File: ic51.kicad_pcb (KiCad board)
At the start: 2 copper layers, 76.1 x 76 mm, 5 parts, among them J1 Conn_02x18_Odd_Even, J2 Conn_02x18_Odd_Even, J3 Conn_02x18_Odd_Even, J4 Conn_02x18_Odd_Even, U1 ic51-1444-schem

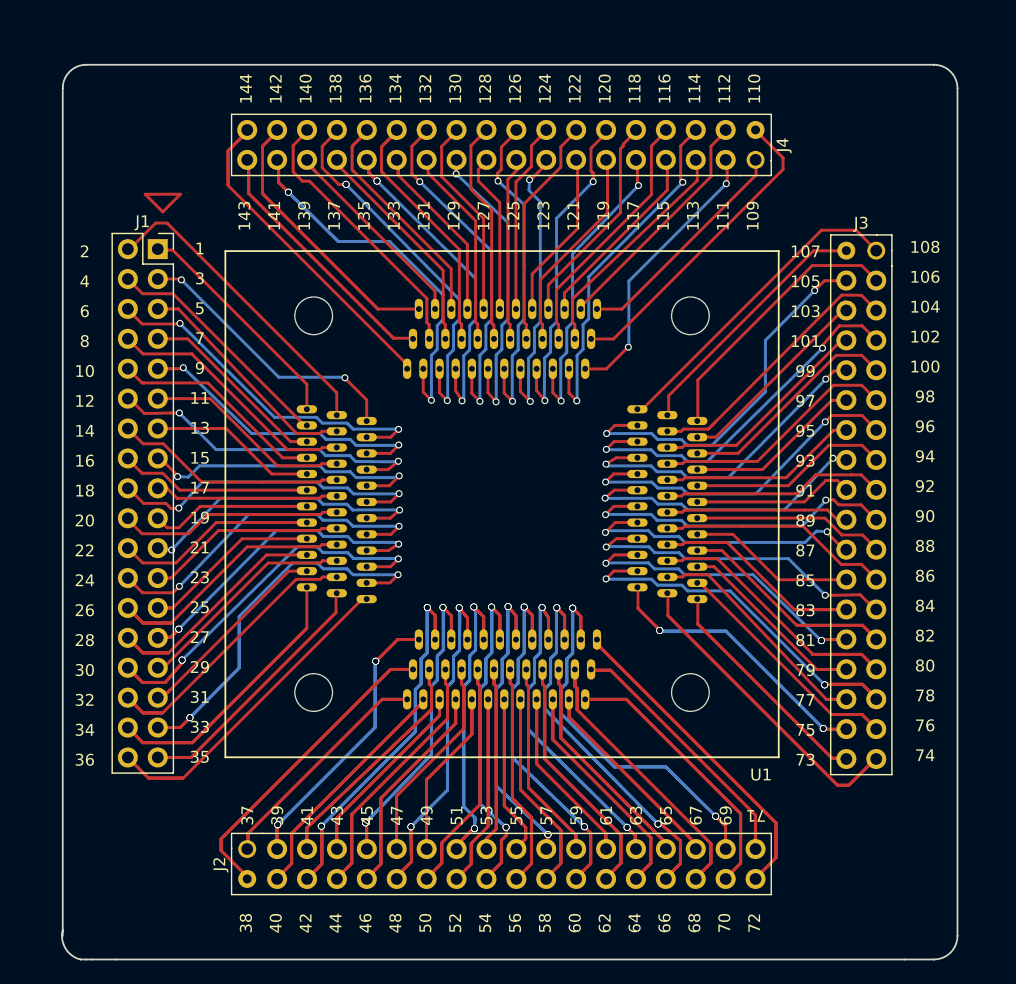
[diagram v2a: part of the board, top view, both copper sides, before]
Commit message: fill unused zones with copper, move align text properly
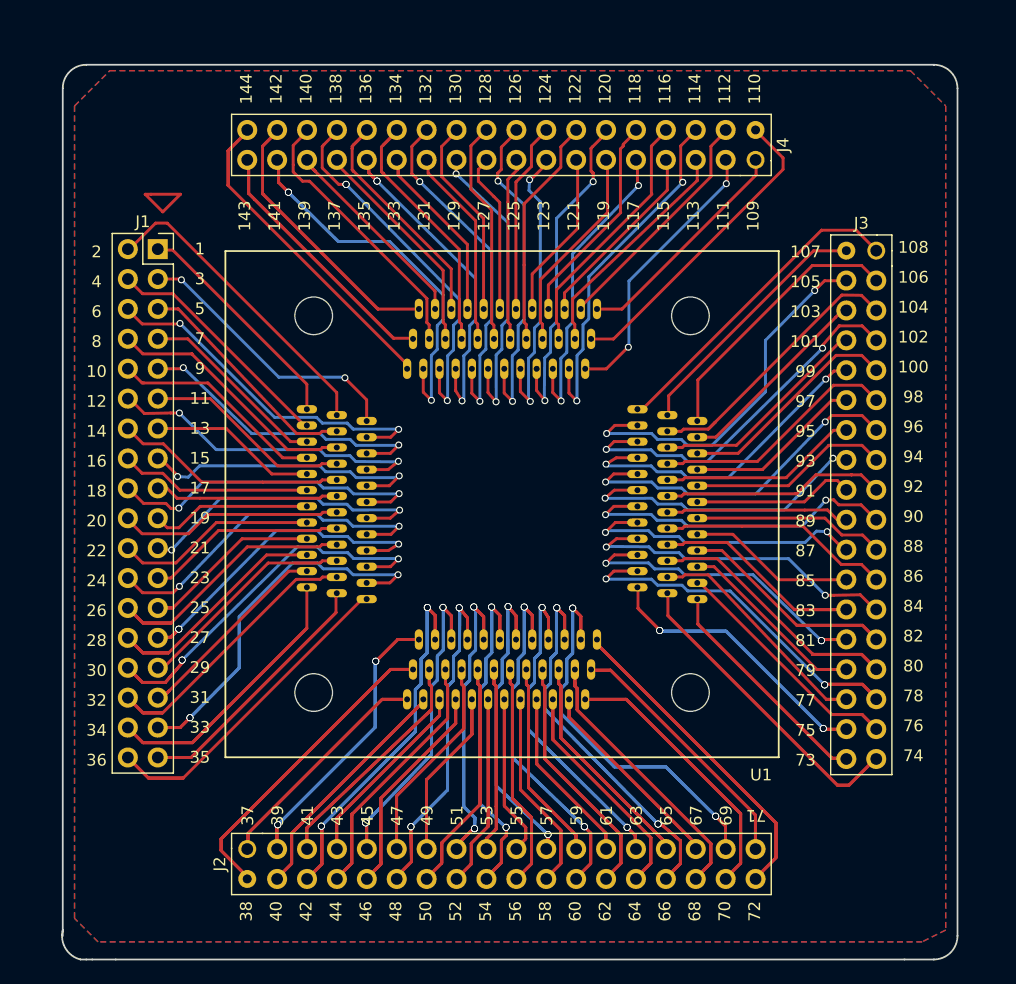
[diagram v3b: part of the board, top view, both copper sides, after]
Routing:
- added copper zone on B.Cu, net (none)
- added copper zone on F.Cu, net (none)
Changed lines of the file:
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@@
     (links 144)
     (no_connects 0)
-    (area -111.414286 -111.414286 213.909502 133.042382)
+    (area 108.863446 56.424999 185.075001 132.575001)
     (thickness 1.6)
     (drawings 159)
@@
     (effects (font (size 1 1) (thickness 0.1)))
   )
-  (gr_text 74 (at 182.25 115.19) (layer F.SilkS)
+  (gr_text 74 (at 181.25 115.19) (layer F.SilkS)
     (effects (font (size 1 1) (thickness 0.1)))
   )
-  (gr_text 76 (at 182.25 112.65) (layer F.SilkS)
+  (gr_text 76 (at 181.25 112.65) (layer F.SilkS)
     (effects (font (size 1 1) (thickness 0.1)))
   )
-  (gr_text 78 (at 182.25 110.11) (layer F.SilkS)
+  (gr_text 78 (at 181.25 110.11) (layer F.SilkS)
     (effects (font (size 1 1) (thickness 0.1)))
   )
-  (gr_text 80 (at 182.25 107.57) (layer F.SilkS)
+  (gr_text 80 (at 181.25 107.57) (layer F.SilkS)
     (effects (font (size 1 1) (thickness 0.1)))
   )
-  (gr_text 82 (at 182.25 105.03) (layer F.SilkS)
+  (gr_text 82 (at 181.25 105.03) (layer F.SilkS)
     (effects (font (size 1 1) (thickness 0.1)))
   )
-  (gr_text 84 (at 182.25 102.49) (layer F.SilkS)
+  (gr_text 84 (at 181.25 102.49) (layer F.SilkS)
     (effects (font (size 1 1) (thickness 0.1)))
   )
-  (gr_text 86 (at 182.25 99.95) (layer F.SilkS)
+  (gr_text 86 (at 181.25 99.95) (layer F.SilkS)
     (effects (font (size 1 1) (thickness 0.1)))
   )
-  (gr_text 88 (at 182.25 97.41) (layer F.SilkS)
+  (gr_text 88 (at 181.25 97.41) (layer F.SilkS)
     (effects (font (size 1 1) (thickness 0.1)))
   )
-  (gr_text 90 (at 182.25 94.87) (layer F.SilkS)
+  (gr_text 90 (at 181.25 94.87) (layer F.SilkS)
     (effects (font (size 1 1) (thickness 0.1)))
   )
-  (gr_text 92 (at 182.25 92.33) (layer F.SilkS)
+  (gr_text 92 (at 181.25 92.33) (layer F.SilkS)
     (effects (font (size 1 1) (thickness 0.1)))
   )
-  (gr_text 94 (at 182.25 89.79) (layer F.SilkS)
+  (gr_text 94 (at 181.25 89.79) (layer F.SilkS)
     (effects (font (size 1 1) (thickness 0.1)))
   )
-  (gr_text 96 (at 182.25 87.25) (layer F.SilkS)
+  (gr_text 96 (at 181.25 87.25) (layer F.SilkS)
     (effects (font (size 1 1) (thickness 0.1)))
   )
-  (gr_text 98 (at 182.25 84.71) (layer F.SilkS)
+  (gr_text 98 (at 181.25 84.71) (layer F.SilkS)
     (effects (font (size 1 1) (thickness 0.1)))
   )
-  (gr_text 100 (at 182.25 82.17) (layer F.SilkS)
+  (gr_text 100 (at 181.25 82.17) (layer F.SilkS)
     (effects (font (size 1 1) (thickness 0.1)))
   )
-  (gr_text 102 (at 182.25 79.63) (layer F.SilkS)
+  (gr_text 102 (at 181.25 79.63) (layer F.SilkS)
     (effects (font (size 1 1) (thickness 0.1)))
   )
-  (gr_text 104 (at 182.25 77.09) (layer F.SilkS)
+  (gr_text 104 (at 181.25 77.09) (layer F.SilkS)
     (effects (font (size 1 1) (thickness 0.1)))
   )
-  (gr_text 106 (at 182.25 74.55) (layer F.SilkS)
+  (gr_text 106 (at 181.25 74.55) (layer F.SilkS)
     (effects (font (size 1 1) (thickness 0.1)))
   )
-  (gr_text 108 (at 182.25 72.01) (layer F.SilkS)
+  (gr_text 108 (at 181.25 72.01) (layer F.SilkS)
     (effects (font (size 1 1) (thickness 0.1)))
   )
@@
     (effects (font (size 1 1) (thickness 0.1)))
   )
-  (gr_text 72 (at 167.77 129.41 90) (layer F.SilkS)
+  (gr_text 72 (at 167.77 128.41 90) (layer F.SilkS)
     (effects (font (size 1 1) (thickness 0.1)))
   )
-  (gr_text 70 (at 165.23 129.41 90) (layer F.SilkS)
+  (gr_text 70 (at 165.23 128.41 90) (layer F.SilkS)
     (effects (font (size 1 1) (thickness 0.1)))
   )
-  (gr_text 68 (at 162.69 129.41 90) (layer F.SilkS)
+  (gr_text 68 (at 162.69 128.41 90) (layer F.SilkS)
     (effects (font (size 1 1) (thickness 0.1)))
   )
-  (gr_text 66 (at 160.15 129.41 90) (layer F.SilkS)
+  (gr_text 66 (at 160.15 128.41 90) (layer F.SilkS)
     (effects (font (size 1 1) (thickness 0.1)))
   )
-  (gr_text 64 (at 157.61 129.41 90) (layer F.SilkS)
+  (gr_text 64 (at 157.61 128.41 90) (layer F.SilkS)
     (effects (font (size 1 1) (thickness 0.1)))
   )
-  (gr_text 62 (at 155.07 129.41 90) (layer F.SilkS)
+  (gr_text 62 (at 155.07 128.41 90) (layer F.SilkS)
     (effects (font (size 1 1) (thickness 0.1)))
   )
-  (gr_text 60 (at 152.53 129.41 90) (layer F.SilkS)
+  (gr_text 60 (at 152.53 128.41 90) (layer F.SilkS)
     (effects (font (size 1 1) (thickness 0.1)))
   )
-  (gr_text 58 (at 149.99 129.41 90) (layer F.SilkS)
+  (gr_text 58 (at 149.99 128.41 90) (layer F.SilkS)
     (effects (font (size 1 1) (thickness 0.1)))
   )
-  (gr_text 56 (at 147.45 129.41 90) (layer F.SilkS)
+  (gr_text 56 (at 147.45 128.41 90) (layer F.SilkS)
     (effects (font (size 1 1) (thickness 0.1)))
   )
-  (gr_text 54 (at 144.91 129.41 90) (layer F.SilkS)
+  (gr_text 54 (at 144.91 128.41 90) (layer F.SilkS)
     (effects (font (size 1 1) (thickness 0.1)))
   )
-  (gr_text 52 (at 142.37 129.41 90) (layer F.SilkS)
+  (gr_text 52 (at 142.37 128.41 90) (layer F.SilkS)
     (effects (font (size 1 1) (thickness 0.1)))
   )
-  (gr_text 50 (at 139.83 129.41 90) (layer F.SilkS)
+  (gr_text 50 (at 139.83 128.41 90) (layer F.SilkS)
     (effects (font (size 1 1) (thickness 0.1)))
   )
-  (gr_text 48 (at 137.29 129.41 90) (layer F.SilkS)
+  (gr_text 48 (at 137.29 128.41 90) (layer F.SilkS)
     (effects (font (size 1 1) (thickness 0.1)))
   )
-  (gr_text 46 (at 134.75 129.41 90) (layer F.SilkS)
+  (gr_text 46 (at 134.75 128.41 90) (layer F.SilkS)
     (effects (font (size 1 1) (thickness 0.1)))
   )
-  (gr_text 44 (at 132.21 129.41 90) (layer F.SilkS)
+  (gr_text 44 (at 132.21 128.41 90) (layer F.SilkS)
     (effects (font (size 1 1) (thickness 0.1)))
   )
-  (gr_text 42 (at 129.67 129.41 90) (layer F.SilkS)
+  (gr_text 42 (at 129.67 128.41 90) (layer F.SilkS)
     (effects (font (size 1 1) (thickness 0.1)))
   )
-  (gr_text 40 (at 127.13 129.41 90) (layer F.SilkS)
+  (gr_text 40 (at 127.13 128.41 90) (layer F.SilkS)
     (effects (font (size 1 1) (thickness 0.1)))
   )
-  (gr_text 38 (at 124.59 129.41 90) (layer F.SilkS)
+  (gr_text 38 (at 124.59 128.41 90) (layer F.SilkS)
     (effects (font (size 1 1) (thickness 0.1)))
   )
@@
     (effects (font (size 1 1) (thickness 0.1)))
   )
-  (gr_text 36 (at 110.87 115.57) (layer F.SilkS)
+  (gr_text 36 (at 111.87 115.57) (layer F.SilkS)
     (effects (font (size 1 1) (thickness 0.1)))
   )
-  (gr_text 34 (at 110.87 113.03) (layer F.SilkS)
+  (gr_text 34 (at 111.87 113.03) (layer F.SilkS)
     (effects (font (size 1 1) (thickness 0.1)))
   )
-  (gr_text 32 (at 110.87 110.49) (layer F.SilkS)
+  (gr_text 32 (at 111.87 110.49) (layer F.SilkS)
     (effects (font (size 1 1) (thickness 0.1)))
   )
-  (gr_text 30 (at 110.87 107.95) (layer F.SilkS)
+  (gr_text 30 (at 111.87 107.95) (layer F.SilkS)
     (effects (font (size 1 1) (thickness 0.1)))
   )
-  (gr_text 28 (at 110.87 105.41) (layer F.SilkS)
+  (gr_text 28 (at 111.87 105.41) (layer F.SilkS)
     (effects (font (size 1 1) (thickness 0.1)))
   )
-  (gr_text 26 (at 110.87 102.87) (layer F.SilkS)
+  (gr_text 26 (at 111.87 102.87) (layer F.SilkS)
     (effects (font (size 1 1) (thickness 0.1)))
   )
-  (gr_text 24 (at 110.87 100.33) (layer F.SilkS)
+  (gr_text 24 (at 111.87 100.33) (layer F.SilkS)
     (effects (font (size 1 1) (thickness 0.1)))
   )
-  (gr_text 22 (at 110.87 97.79) (layer F.SilkS)
+  (gr_text 22 (at 111.87 97.79) (layer F.SilkS)
     (effects (font (size 1 1) (thickness 0.1)))
   )
-  (gr_text 20 (at 110.87 95.25) (layer F.SilkS)
+  (gr_text 20 (at 111.87 95.25) (layer F.SilkS)
     (effects (font (size 1 1) (thickness 0.1)))
   )
-  (gr_text 18 (at 110.87 92.71) (layer F.SilkS)
+  (gr_text 18 (at 111.87 92.71) (layer F.SilkS)
     (effects (font (size 1 1) (thickness 0.1)))
   )
-  (gr_text 16 (at 110.87 90.17) (layer F.SilkS)
+  (gr_text 16 (at 111.87 90.17) (layer F.SilkS)
     (effects (font (size 1 1) (thickness 0.1)))
   )
-  (gr_text 14 (at 110.87 87.63) (layer F.SilkS)
+  (gr_text 14 (at 111.87 87.63) (layer F.SilkS)
     (effects (font (size 1 1) (thickness 0.1)))
   )
-  (gr_text 12 (at 110.87 85.09) (layer F.SilkS)
+  (gr_text 12 (at 111.87 85.09) (layer F.SilkS)
     (effects (font (size 1 1) (thickness 0.1)))
   )
-  (gr_text 10 (at 110.87 82.55) (layer F.SilkS)
+  (gr_text 10 (at 111.87 82.55) (layer F.SilkS)
     (effects (font (size 1 1) (thickness 0.1)))
   )
-  (gr_text 8 (at 110.87 80.01) (layer F.SilkS)
+  (gr_text 8 (at 111.87 80.01) (layer F.SilkS)
     (effects (font (size 1 1) (thickness 0.1)))
   )
-  (gr_text 6 (at 110.87 77.47) (layer F.SilkS)
+  (gr_text 6 (at 111.87 77.47) (layer F.SilkS)
     (effects (font (size 1 1) (thickness 0.1)))
   )
-  (gr_text 4 (at 110.87 74.93) (layer F.SilkS)
+  (gr_text 4 (at 111.87 74.93) (layer F.SilkS)
     (effects (font (size 1 1) (thickness 0.1)))
   )
-  (gr_text 2 (at 110.87 72.39) (layer F.SilkS)
+  (gr_text 2 (at 111.87 72.39) (layer F.SilkS)
     (effects (font (size 1 1) (thickness 0.1)))
   )
@@
   (segment (start 162.942959 104.009889) (end 162.942959 101.88239) (width 0.25) (layer F.Cu) (net 144))
   (segment (start 175.52796 115.40489) (end 175.60796 115.48489) (width 0.25) (layer F.Cu) (net 144))
+  (zone (net 0) (net_name "") (layer F.Cu) (hatch edge 0.508)
+    (connect_pads (clearance 0.508))
+    (min_thickness 0.254)
+    (fill yes (arc_segments 16) (thermal_gap 0.508) (thermal_bridge_width 0.508))
+    (polygon
+      (pts
+        (xy 184 60) (xy 184 130) (xy 182 131) (xy 112 131) (xy 110 129)
+        (xy 110 60) (xy 113 57) (xy 181 57)
+      )
+    )
+  )
+  (zone (net 0) (net_name "") (layer B.Cu) (hatch edge 0.508)
+    (connect_pads (clearance 0.508))
+    (min_thickness 0.254)
+    (fill yes (arc_segments 16) (thermal_gap 0.508) (thermal_bridge_width 0.508))
+    (polygon
+      (pts
+        (xy 184 60) (xy 184 130) (xy 182 131) (xy 112 131) (xy 110 129)
+        (xy 110 60) (xy 113 57) (xy 181 57)
+      )
+    )
+  )
 )

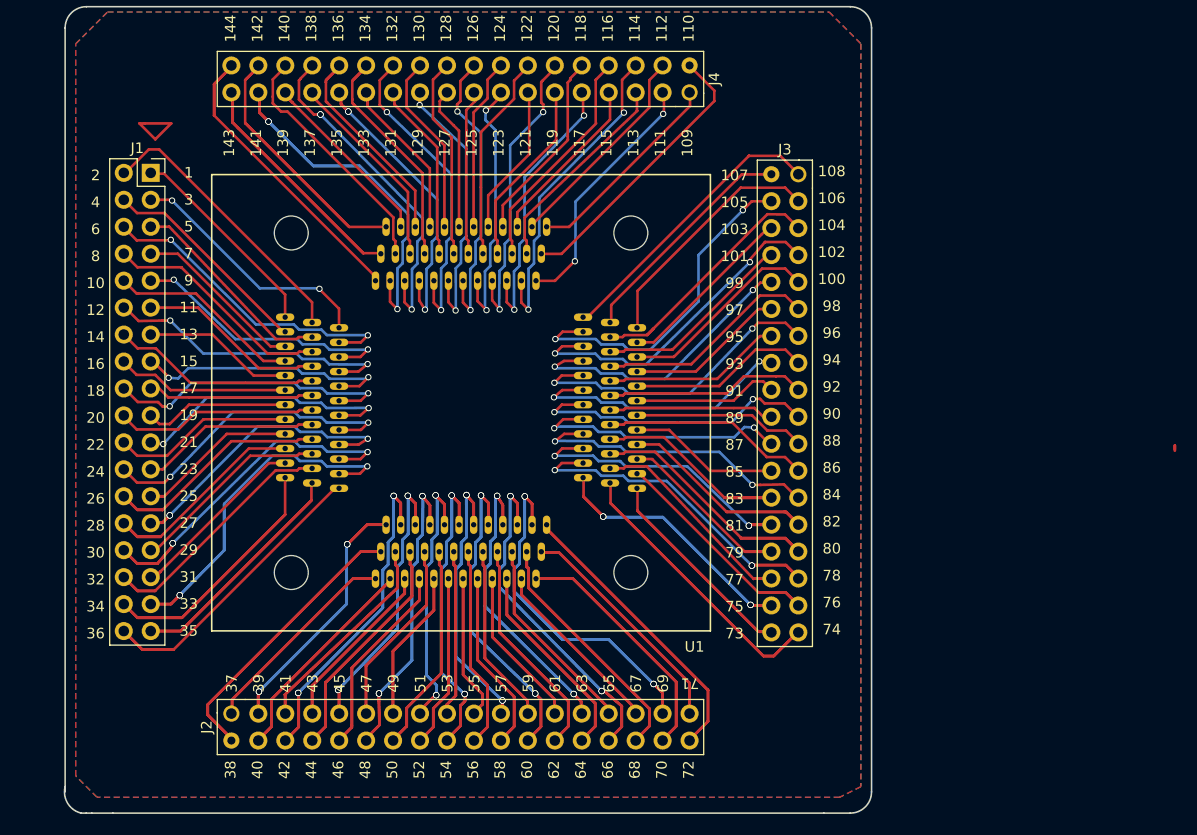
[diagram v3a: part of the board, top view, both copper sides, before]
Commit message: remove redundant vias as it is pcb-house, swap top and bottom cu
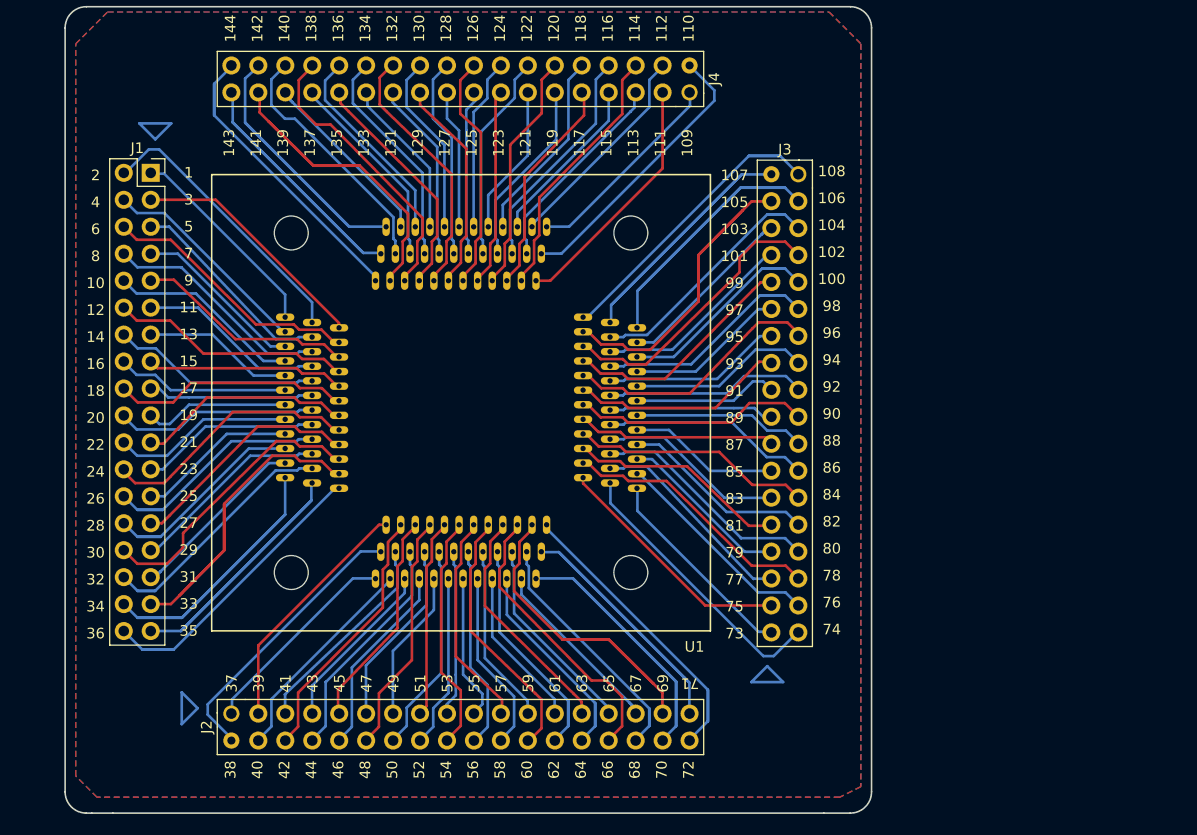
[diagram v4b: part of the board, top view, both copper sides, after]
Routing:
- net /66: track 63.7 -> 27.1 mm, vias 4 -> 0
- net /42: track 61.0 -> 24.8 mm, vias 4 -> 0
- net /60: track 59.7 -> 24.5 mm, vias 4 -> 0
- net /54: track 56.3 -> 22.3 mm, vias 4 -> 0
- net /48: track 56.3 -> 22.8 mm, vias 4 -> 0
- net /63: track 55.1 -> 22.7 mm, vias 4 -> 0
- net /51: track 50.9 -> 18.7 mm, vias 4 -> 0
- net /57: track 52.4 -> 20.4 mm, vias 4 -> 0
- net /45: track 52.6 -> 20.7 mm, vias 4 -> 0
- net /69: track 65.0 -> 37.1 mm, vias 4 -> 0
- net /38: track 52.9 -> 26.5 mm
- net /72: track 55.7 -> 30.8 mm
- net /39: track 48.0 -> 23.3 mm, vias 4 -> 0
- net /74: track 51.0 -> 26.5 mm
- net /75: track 46.2 -> 23.1 mm, vias 4 -> 0
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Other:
- board size 76.1 x 76 mm -> 76 x 76 mm

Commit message: some changes due to panelizing
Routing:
- net (no net): track 21.7 -> 0.00 mm
- net /34: track 41.2 -> 22.2 mm
- net /70: track 41.2 -> 22.4 mm
- net /106: track 41.2 -> 22.6 mm
- net /35: track 39.5 -> 21.1 mm
- net /71: track 39.5 -> 21.4 mm
- net /107: track 39.5 -> 21.4 mm
- net /143: track 39.5 -> 21.7 mm
- net /142: track 37.2 -> 22.8 mm
- net /36: track 30.8 -> 27.5 mm
- net /72: track 30.8 -> 27.8 mm
- net /108: track 30.8 -> 27.8 mm
- net /144: track 30.8 -> 27.8 mm
- net /74: track 26.5 -> 25.2 mm
- net /38: track 26.5 -> 25.5 mm
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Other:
- outline, holes or cut-outs redrawn
- board text added: "V.01"
